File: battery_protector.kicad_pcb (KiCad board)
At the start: 4 copper layers, 0 parts

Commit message: setup layout rules
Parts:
- added C1: 150nF X7R, Capacitor_SMD:C_0603_1608Metric, F.Cu at (134.8, 95.0)
- added C10: 1uF, Capacitor_SMD:C_0603_1608Metric, F.Cu at (155.9, 101.9)
- added C11: 1u, Capacitor_SMD:C_0603_1608Metric, F.Cu at (115.8, 75.4)
- added C12: 10u, Capacitor_SMD:C_0603_1608Metric, F.Cu at (115.8, 77.9)
- added C13: 0.1u, Capacitor_SMD:C_0603_1608Metric, F.Cu at (115.8, 80.4)
- added C14: 1u, Capacitor_SMD:C_0603_1608Metric, F.Cu at (115.8, 83.0)
- added C15: 10uF, Capacitor_SMD:C_0603_1608Metric, F.Cu at (115.8, 85.5)
- added C16: 100nF, Capacitor_SMD:C_0603_1608Metric, F.Cu at (115.8, 88.0)
- added C17: 10nF, Capacitor_SMD:C_0603_1608Metric, F.Cu at (151.9, 114.0)
- added C18: 220nF, Capacitor_SMD:C_0603_1608Metric, F.Cu at (151.9, 116.5)
- added C19: 2.2uF, Capacitor_SMD:C_0603_1608Metric, F.Cu at (151.9, 119.0)
- added C2: 1n, Capacitor_SMD:C_0603_1608Metric, F.Cu at (151.9, 96.9)
- added C20: 220nF, Capacitor_SMD:C_0603_1608Metric, F.Cu at (151.9, 121.5)
- added C21: 4.7uF, Capacitor_SMD:C_0603_1608Metric, F.Cu at (151.9, 124.0)
- added C3: 4.7u, Capacitor_SMD:C_0603_1608Metric, F.Cu at (151.9, 99.4)
- added C4: 100n, Capacitor_SMD:C_0603_1608Metric, F.Cu at (151.9, 101.9)
- added C5: 10u, Capacitor_SMD:C_0603_1608Metric, F.Cu at (151.9, 104.5)
- added C6: 100n, Capacitor_SMD:C_0603_1608Metric, F.Cu at (151.9, 107.0)
- added C7: 47u, Capacitor_SMD:C_0603_1608Metric, F.Cu at (151.9, 109.5)
- added C8: 47u, Capacitor_SMD:C_0603_1608Metric, F.Cu at (155.9, 96.9)
- added C9: 1uF, Capacitor_SMD:C_0603_1608Metric, F.Cu at (155.9, 99.4)
- added D1: LED, LED_SMD:LED_0603_1608Metric, F.Cu at (176.7, 48.9)
- added D10: STPS3L60U, custom_footprints:STPS3L60U, F.Cu at (171.1, 84.2)
- added D11: D_TVS, Diode_SMD:D_0402_1005Metric, F.Cu at (175.3, 96.7)
- added D12: 1N5819, custom_footprints:1N5819HW-7-F, F.Cu at (164.7, 107.3)
- added D13: D_TVS, Diode_SMD:D_0402_1005Metric, F.Cu at (175.3, 98.7)
- added D14: D_TVS, Diode_SMD:D_0402_1005Metric, F.Cu at (175.3, 100.6)
- added D15: D_Schottky_AAK, custom_footprints:VB30100S-E38W, F.Cu at (133.1, 115.5)
- added D2: LED, LED_SMD:LED_0603_1608Metric, F.Cu at (176.7, 51.5)
- added D3: LED, LED_SMD:LED_0603_1608Metric, F.Cu at (176.7, 54.1)
- added D4: LED, LED_SMD:LED_0603_1608Metric, F.Cu at (176.7, 56.7)
- added D5: SMCJ51CA, Diode_SMD:D_SMC, F.Cu at (127.4, 97.6)
- added D6: STPS3L60U, custom_footprints:STPS3L60U, F.Cu at (127.6, 124.4)
- added D7: STPS3L60U, custom_footprints:STPS3L60U, F.Cu at (127.6, 130.0)
- added D8: SMCJ51CA, Diode_SMD:D_SMC, F.Cu at (127.4, 105.4)
- added H5: MountingHole_Pad, MountingHole:MountingHole_3.2mm_M3_Pad_TopBottom, F.Cu at (152.5, 51.1)
- added H6: MountingHole_Pad, MountingHole:MountingHole_3.2mm_M3_Pad_TopBottom, F.Cu at (152.5, 59.1)
- added H7: MountingHole_Pad, MountingHole:MountingHole_3.2mm_M3_Pad_TopBottom, F.Cu at (152.5, 67.0)
- added H8: MountingHole_Pad, MountingHole:MountingHole_3.2mm_M3_Pad_TopBottom, F.Cu at (152.5, 75.0)
- added J1: TB005-762-02BE, custom_footprints:CUI_TB005-762-02BE, F.Cu at (162.4, 54.0)
- added J2: TB005-762-02BE, custom_footprints:CUI_TB005-762-02BE, F.Cu at (162.4, 69.1)
- added J3: USB_C_Receptacle_USB2.0_16P, Connector_USB:USB_C_Receptacle_GCT_USB4105-xx-A_16P_TopMnt_Horizontal, F.Cu at (167.7, 101.0)
- added J5: Conn_01x12, Connector_PinHeader_2.54mm:PinHeader_1x12_P2.54mm_Vertical, F.Cu at (105.5, 50.6)
- added L1: 15u, Inductor_SMD:L_Bourns_SRR1208_12.7x12.7mm, F.Cu at (157.7, 88.5)
- added Q1: SQJQ184ER, custom_footprints:SQJQ184ER, F.Cu at (115.5, 98.6)
- added Q2: SQJQ184ER, custom_footprints:SQJQ184ER, F.Cu at (115.5, 108.2)
- added Q3: SQJQ184ER, custom_footprints:SQJQ184ER, F.Cu at (115.5, 117.9)
- added Q4: SQJQ184ER, custom_footprints:SQJQ184ER, F.Cu at (115.5, 127.6)
- added Q5: MMBT3904, Package_TO_SOT_SMD:SOT-23, F.Cu at (138.2, 82.8)
- added Q6: MMBT3904, Package_TO_SOT_SMD:SOT-23, F.Cu at (138.2, 87.5)
- added R1: 2.2k, Resistor_SMD:R_0603_1608Metric, F.Cu at (176.6, 59.2)
- added R10: 100, Resistor_SMD:R_0603_1608Metric, F.Cu at (138.8, 95.0)
- added R11: 100, Resistor_SMD:R_0603_1608Metric, F.Cu at (138.8, 97.5)
- added R12: 150k, Resistor_SMD:R_0603_1608Metric, F.Cu at (138.8, 100.0)
- added R13: 150k, Resistor_SMD:R_0603_1608Metric, F.Cu at (138.8, 102.5)
- added R14: 1k, Resistor_SMD:R_0603_1608Metric, F.Cu at (138.8, 105.0)
- added R15: 5.1k, Resistor_SMD:R_0603_1608Metric, F.Cu at (155.9, 104.5)
- added R16: 5.1k, Resistor_SMD:R_0603_1608Metric, F.Cu at (155.9, 107.0)
- added R17: 330k, Resistor_SMD:R_0603_1608Metric, F.Cu at (155.9, 109.5)
- added R18: 200k, Resistor_SMD:R_0603_1608Metric, F.Cu at (159.9, 96.9)
- added R19: 63.4k, Resistor_SMD:R_0603_1608Metric, F.Cu at (159.9, 99.4)
- added R2: 5.1k, Resistor_SMD:R_0603_1608Metric, F.Cu at (176.6, 61.7)
- added R20: 40.2k, Resistor_SMD:R_0603_1608Metric, F.Cu at (159.9, 101.9)
- added R21: 10k, Resistor_SMD:R_0603_1608Metric, F.Cu at (159.9, 104.5)
- added R22: 10k, Resistor_SMD:R_0603_1608Metric, F.Cu at (159.9, 107.0)
- added R23: 22.1k, Resistor_SMD:R_0603_1608Metric, F.Cu at (115.8, 90.5)
- added R24: 47.5k, Resistor_SMD:R_0603_1608Metric, F.Cu at (119.8, 75.4)
- added R25: 10k, Resistor_SMD:R_0603_1608Metric, F.Cu at (119.8, 77.9)
- added R26: 1k, Resistor_SMD:R_0603_1608Metric, F.Cu at (119.8, 80.4)
- added R27: 10k, Resistor_SMD:R_0603_1608Metric, F.Cu at (119.8, 83.0)
- added R28: 5.1k, Resistor_SMD:R_0603_1608Metric, F.Cu at (119.8, 85.5)
- added R29: 5.1k, Resistor_SMD:R_0603_1608Metric, F.Cu at (119.8, 88.0)
- added R3: 2.2k, Resistor_SMD:R_0603_1608Metric, F.Cu at (176.6, 64.3)
- added R30: 10k, Resistor_SMD:R_0603_1608Metric, F.Cu at (119.8, 90.5)
- added R31: 10k, Resistor_SMD:R_0603_1608Metric, F.Cu at (123.8, 75.4)
- added R32: 0, Resistor_SMD:R_0603_1608Metric, F.Cu at (123.8, 77.9)
- added R33: 0, Resistor_SMD:R_0603_1608Metric, F.Cu at (123.8, 80.4)
- added R34: 75k, Resistor_SMD:R_0603_1608Metric, F.Cu at (123.8, 83.0)
- added R35: 5.1k, Resistor_SMD:R_0603_1608Metric, F.Cu at (123.8, 85.5)
- added R36: 10k, Resistor_SMD:R_0603_1608Metric, F.Cu at (155.9, 114.0)
- added R37: 1k, Resistor_SMD:R_0603_1608Metric, F.Cu at (155.9, 116.5)
- added R38: 1k, Resistor_SMD:R_0603_1608Metric, F.Cu at (155.9, 119.0)
- added R39: 1k, Resistor_SMD:R_0603_1608Metric, F.Cu at (155.9, 121.5)
- added R4: 5.1k, Resistor_SMD:R_0603_1608Metric, F.Cu at (176.6, 66.8)
- added R40: 1k, Resistor_SMD:R_0603_1608Metric, F.Cu at (155.9, 124.0)
- added R41: 1k, Resistor_SMD:R_0603_1608Metric, F.Cu at (159.9, 114.0)
- added R42: 1k, Resistor_SMD:R_0603_1608Metric, F.Cu at (159.9, 116.5)
- added R43: 1k, Resistor_SMD:R_0603_1608Metric, F.Cu at (159.9, 119.0)
- added R5: 10, Resistor_SMD:R_0603_1608Metric, F.Cu at (134.8, 97.5)
- added R6: 1m 1% 3W, custom_footprints:WSK12161L000FEA, F.Cu at (134.2, 124.5)
- added R7: 10, Resistor_SMD:R_0603_1608Metric, F.Cu at (134.8, 100.0)
- added R8: 10, Resistor_SMD:R_0603_1608Metric, F.Cu at (134.8, 102.5)
- added R9: 10, Resistor_SMD:R_0603_1608Metric, F.Cu at (134.8, 105.0)
- added SW1: SW_DPDT_x2, Button_Switch_THT:SW_CK_JS202011CQN_DPDT_Straight, F.Cu at (138.5, 75.7)
- added SW2: PTS647SN50SMTR2_LFS, custom_footprints:PTS647SK50SMTR2LFS, F.Cu at (130.8, 78.0)
- added SW3: PTS647SN50SMTR2_LFS, custom_footprints:PTS647SK50SMTR2LFS, F.Cu at (130.8, 85.6)
- added U1: LMR38020SDDAR, Package_SO:Texas_R-PDSO-G8_EP2.95x4.9mm_Mask2.4x3.1mm, F.Cu at (169.7, 90.4)
- added U2: AP2112K-3.3, Package_TO_SOT_SMD:SOT-23-5, F.Cu at (170.1, 108.1)
- added U3: TPS2116DRL, Package_TO_SOT_SMD:SOT-583-8, F.Cu at (174.5, 107.7)
- added U4: CP2102N-Axx-xQFN28, Package_DFN_QFN:QFN-28-1EP_5x5mm_P0.5mm_EP3.35x3.35mm, F.Cu at (144.2, 84.1)
- added U5: ESP32-C3-WROOM-02, custom_footprints:ESP32-C3-WROOM, F.Cu at (128.6, 66.5)
- added U6: LIS3DH, Package_LGA:LGA-16_3x3mm_P0.5mm_LayoutBorder3x5y, F.Cu at (111.5, 82.6)
- added U7: 2ED4820EMXUMA2, custom_footprints:2ed4820emxuma2, F.Cu at (166.6, 117.9)
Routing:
- net GND: vias 0 -> 12
- added copper zone on In1.Cu, net GND
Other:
- board outline added: 140.5 x 121.1 mm

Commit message: first pass layout
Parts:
- added C22: 4.7uF, Capacitor_SMD:C_0603_1608Metric, F.Cu at (192.5, 81.2)
- added C23: 0.1uF, Capacitor_SMD:C_0603_1608Metric, F.Cu at (192.5, 79.7)
- R25, R27, R34, R35: moved to B.Cu
- moved D1 88.1 mm to (89.8, 33.8), turned to 180 degrees
- moved D2 88.0 mm to (89.8, 37.0), turned to 180 degrees
- moved D3 87.9 mm to (89.8, 40.2), turned to 180 degrees
- moved D4 87.8 mm to (89.8, 43.5), turned to 180 degrees
- moved R1 87.3 mm to (93.1, 33.8)
- moved R2 87.1 mm to (93.1, 37.0)
- moved R3 86.9 mm to (93.1, 40.2)
- moved R4 86.7 mm to (93.1, 43.5)
- moved J1 86.7 mm to (91.7, 104.1)
- moved J2 86.7 mm to (91.7, 119.2)
- moved R30 82.9 mm to (195.5, 56.5), turned to 180 degrees
- moved SW3 80.3 mm to (205.9, 57.1)
- moved SW2 80.0 mm to (205.9, 50.4)
- moved C11 79.3 mm to (194.8, 82.4), turned to -90 degrees
- moved C16 77.7 mm to (174.5, 37.0), turned to 90 degrees
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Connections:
- C12 pad 2: GND -> +3V3
- C13 pad 2: GND -> +3V3
- C14 pad 2: GND -> +3V3
- H7 pad 1: GND -> +3V3
- J5 pad 2: /MCU/I2C1_SCL -> +3V3
- R21 pad 1: GND -> +3V3
- R35 pad 1: GND -> +3V3
- U1 pad 1: GND -> +3V3
- U1 pad 9: GND -> +3V3
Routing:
- net GND: track 0.00 -> 41.3 mm, vias 12 -> 34
- net +3V3: track 0.00 -> 19.6 mm, vias 0 -> 5
- net /MCU/I2C1_SCL: track 0.00 -> 17.5 mm, vias 0 -> 2
- net Net-(SW1B-B): track 0.00 -> 16.2 mm
- net Net-(U1-SW): track 0.00 -> 15.1 mm
- net /MCU/CHIP_PU: track 0.00 -> 14.6 mm, vias 0 -> 1
- net /MCU/I2C1_SDA: track 0.00 -> 14.1 mm
- net Net-(SW1A-B): track 0.00 -> 12.7 mm
- net Net-(D10-K): track 0.00 -> 9.97 mm
- net /MCU/48V_ADC: track 0.00 -> 9.03 mm, vias 0 -> 1
- net /MCU/GD_SAFE: track 0.00 -> 8.56 mm
- net Net-(Q5-B): track 0.00 -> 8.21 mm, vias 0 -> 2
- net BAT+: track 0.00 -> 5.35 mm
- net Net-(U4-VBUS): track 0.00 -> 5.31 mm
- net +5V0_board: track 0.00 -> 4.83 mm
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- added copper zone on In2.Cu, net +3V3

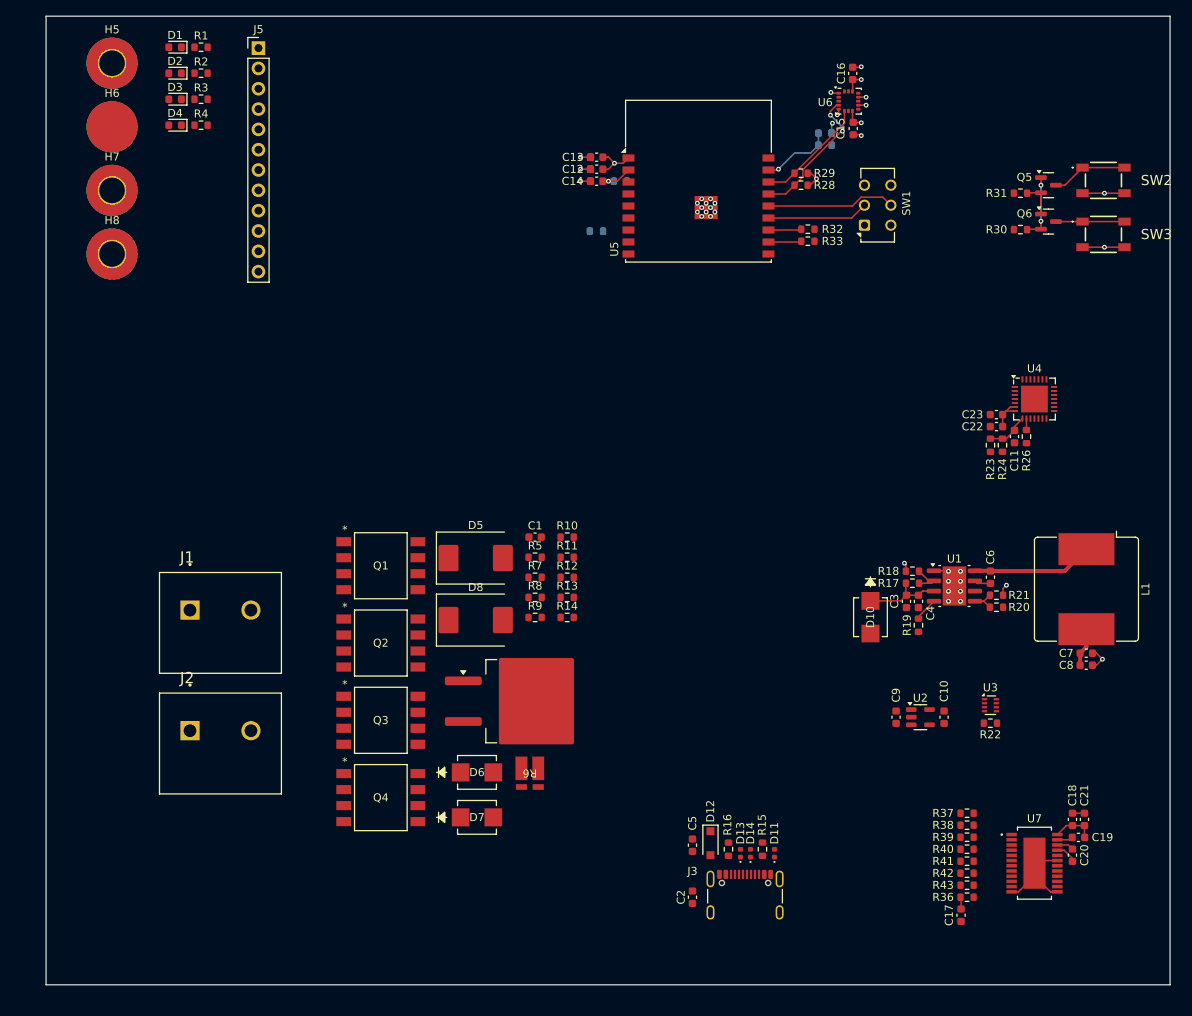
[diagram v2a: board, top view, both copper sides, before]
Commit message: Updated pcb rules and started the rough routing of protection circuitry (#5)
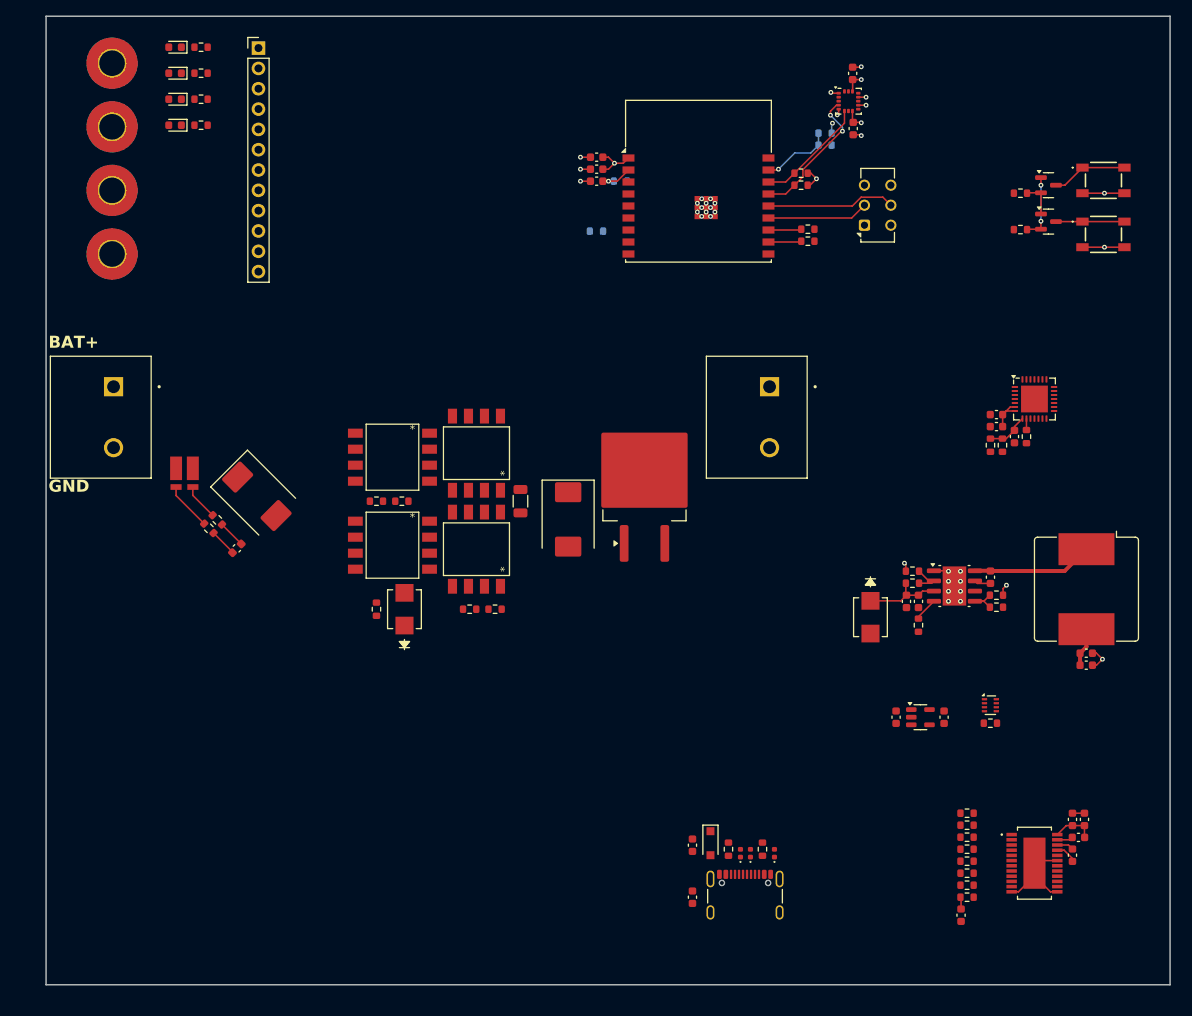
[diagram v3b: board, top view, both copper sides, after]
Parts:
- removed D7: STPS3L60U, custom_footprints:STPS3L60U
- removed R9: 10, Resistor_SMD:R_0603_1608Metric
- R14: footprint Resistor_SMD:R_0603_1608Metric -> Resistor_SMD:R_1206_3216Metric
- moved J2 84.2 mm to (164.1, 76.2), turned to -90 degrees
- moved R6 57.2 mm to (91.0, 87.0)
- moved Q4 44.7 mm to (127.5, 84.5), turned to 90 degrees
- moved R5 40.9 mm to (94.1, 93.9), turned to 135 degrees
- moved R7 40.4 mm to (95.1, 92.8), turned to 135 degrees
- moved C1 37.3 mm to (97.6, 96.4), turned to -135 degrees
- moved D15 31.1 mm to (148.5, 88.5), turned to 90 degrees
- moved J1 29.5 mm to (82.1, 76.2), turned to -90 degrees
- moved D5 28.4 mm to (100.1, 89.9), turned to -45 degrees
- moved Q3 24.5 mm to (127.5, 96.5), turned to 90 degrees
- moved R10 24.3 mm to (115.0, 90.5), turned to 180 degrees
- moved R13 23.9 mm to (118.2, 90.5), turned to 180 degrees
- moved Q2 23.3 mm to (117.0, 85.0), turned to 180 degrees
- moved D6 22.3 mm to (118.5, 104.0), turned to 90 degrees
- moved R8 19.9 mm to (115.0, 104.0), turned to 90 degrees
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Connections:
- C12 pad 2: +3V3 -> GND
- C13 pad 2: +3V3 -> GND
- C14 pad 2: +3V3 -> GND
- H7 pad 1: +3V3 -> GND
- J5 pad 2: +3V3 -> /MCU/I2C1_SCL
- R21 pad 1: +3V3 -> GND
- R35 pad 1: +3V3 -> GND
- R6 pad 1: Net-(D5-A1) -> BAT+
- R6 pad 2: BAT+ -> Net-(D5-A1)
- U1 pad 1: +3V3 -> GND
- U1 pad 9: +3V3 -> GND
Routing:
- net BAT+: track 5.35 -> 11.4 mm
- net Net-(D5-A1): track 0.00 -> 4.55 mm
- net /GateDriver/IS_P: track 0.00 -> 3.45 mm
- net /GateDriver/IS_N: track 0.00 -> 3.42 mm
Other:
- board text added: "BAT+"
- board text added: "GND"

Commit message: Did some more routing
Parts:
- added C24: 1uF, Capacitor_SMD:C_0603_1608Metric, F.Cu at (115.9, 109.6)
- R17: value 330k -> 649k
- R19: value 63.4k -> 64.9k
- R35: value 5.1k -> 3.7k
- moved C21 100.7 mm to (106.8, 101.9), turned to -90 degrees
- moved C19 99.3 mm to (109.1, 99.4), turned to 180 degrees
- moved C18 97.8 mm to (108.3, 101.9), turned to -90 degrees
- moved C20 96.6 mm to (112.1, 99.4), turned to 180 degrees
- moved J3 91.7 mm to (77.4, 103.2), turned to -90 degrees
- moved U7 89.2 mm to (113.8, 104.2), turned to 90 degrees
- moved C2 87.8 mm to (78.2, 96.6), turned to 0 degrees
- moved D11 85.6 mm to (83.7, 106.9), turned to 0 degrees
- moved R37 85.2 mm to (107.2, 105.1)
- moved R38 85.2 mm to (107.2, 106.6)
- moved R39 85.2 mm to (107.2, 108.1)
- moved R40 85.2 mm to (107.2, 109.6)
- moved R41 85.2 mm to (107.2, 111.1)
- moved R42 85.2 mm to (107.2, 112.6)
- moved R43 85.2 mm to (107.2, 114.1)
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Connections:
- D3 pad 2: +5V0 -> +5V0_board
- Q5 pad 2: Net-(Q5-E) -> /MCU/RTS
- Q6 pad 1: Net-(Q5-E) -> Net-(Q6-B)
- Q6 pad 2: Net-(Q5-B) -> /MCU/DTR
- R31 pad 1: Net-(Q5-E) -> Net-(Q6-B)
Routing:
- net GND: track 41.3 -> 51.7 mm, vias 34 -> 38
- net Net-(Q5-E): track 4.41 -> 0.00 mm
- net /MCU/RTS: track 0.00 -> 4.41 mm
- net Net-(U7-CSO): track 0.00 -> 4.02 mm, vias 0 -> 2
- net +3V3: track 19.6 -> 22.9 mm
- net /GateDriver/IS_N: track 3.42 -> 3.66 mm, vias 0 -> 2
- net /GateDriver/IS_P: track 3.45 -> 3.62 mm, vias 0 -> 2
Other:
- board text added: "LOAD+"

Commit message: route dc-dc
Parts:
- moved Q6 134.6 mm to (91.4, 136.3)
- moved R30 134.6 mm to (87.9, 137.3), turned to 0 degrees
- moved Q5 134.6 mm to (91.4, 131.8)
- moved R31 134.6 mm to (87.9, 132.8), turned to 0 degrees
- moved SW2 134.6 mm to (98.2, 131.2)
- moved SW3 134.6 mm to (98.2, 137.9)
- moved R23 125.1 mm to (84.5, 147.8)
- moved R24 125.1 mm to (86.0, 147.8)
- moved U4 125.1 mm to (90.0, 142.0)
- moved C11 125.1 mm to (87.5, 146.7)
- moved C22 125.1 mm to (85.2, 145.5)
- moved C23 125.1 mm to (85.2, 144.0)
- moved R26 125.1 mm to (89.0, 146.7)
- moved C16 112.7 mm to (134.4, 142.4), turned to 0 degrees
- moved U6 110.1 mm to (130.9, 141.9), turned to -90 degrees
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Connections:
- Q6 pad 3: /MCU/GD_SAFE -> /MCU/~{GD_SAFE}
- SW3 pad 1: /MCU/GD_SAFE -> /MCU/~{GD_SAFE}
- SW3 pad 2: /MCU/GD_SAFE -> /MCU/~{GD_SAFE}
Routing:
- net +5V0: track 0.00 -> 33.2 mm, vias 0 -> 2
- net Net-(Q1-G): track 0.00 -> 32.5 mm, vias 0 -> 2
- net /GateDriver/SOURCE_B: track 0.00 -> 31.3 mm
- net GND: track 51.7 -> 82.0 mm, vias 38 -> 58
- net Net-(D6-A): track 0.00 -> 20.5 mm
- net +5V0_board: track 4.83 -> 23.9 mm, vias 0 -> 2
- net Net-(J3-SHIELD): track 0.00 -> 19.0 mm
- net /MCU/~{GD_SAFE}: track 0.00 -> 18.9 mm
- net /DC-DC/USB_DN: track 0.00 -> 16.8 mm, vias 0 -> 2
- net /DC-DC/USB_DP: track 0.00 -> 14.5 mm, vias 0 -> 2
- net /~{CS}: track 0.00 -> 13.4 mm, vias 0 -> 1
- net Net-(D11-A1): track 0.00 -> 12.5 mm
- net /MOSI: track 0.00 -> 12.0 mm
- net +5V0_USB: track 0.00 -> 11.5 mm
- net /MISO: track 0.00 -> 10.8 mm, vias 0 -> 2
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- added copper zone on B.Cu, net /GateDriver/SOURCE_A
- added copper zone on F.Cu, net /GateDriver/SOURCE_A
- added copper zone on B.Cu, net BAT+
- added copper zone on F.Cu, net BAT+
- added copper zone on B.Cu, net GND
- added copper zone on F.Cu, net GND
- added copper zone on B.Cu, net LOAD+
- added copper zone on F.Cu, net LOAD+
- added copper zone on B.Cu, net Net-(D5-A1)
- added copper zone on F.Cu, net Net-(D5-A1)
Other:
- board size 140.5 x 121.1 mm -> 93.7 x 93.8 mm
- board text added: "Automatic ORing 5V->3.3V LDO"
- board text added: "BAT+->5V Buck"
- board text added: "ESP32 MCU"
- board text added: "Gate Driver"
- board text added: "USB-C"
- board text added: "USB-UART Bridge"
